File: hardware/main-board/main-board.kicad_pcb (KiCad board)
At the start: 4 copper layers, 105 x 38 mm, 99 parts, among them J1 USB_C_Receptacle_USB2.0, J2 DNI, J3 Display Connector, J4 Conn_01x04, SW1 SW_Push, SW2 SW_Push, SW3 SW_Push, SW4 SW_Push, SW5 SW_Detect, SW6 SW_Boot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

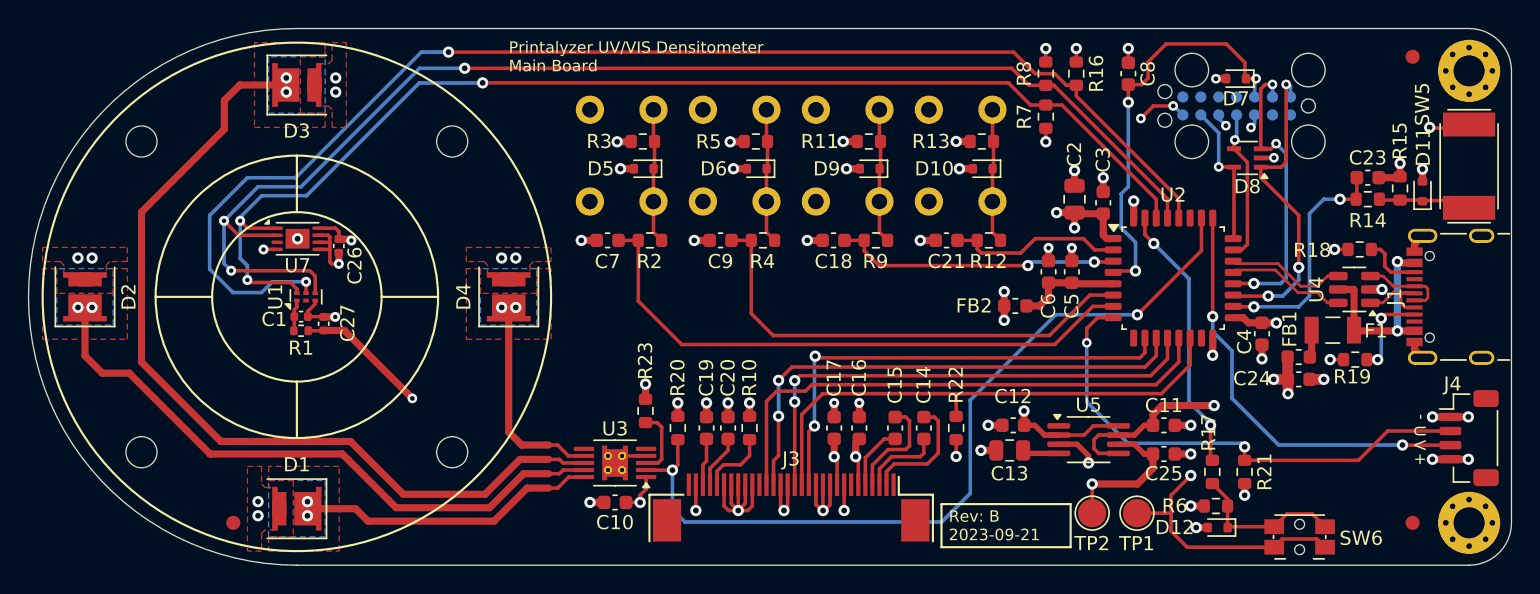
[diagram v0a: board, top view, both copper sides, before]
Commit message: Update main board to match common conventions from current projects
Changed all single-line TVS diodes to the ESD321
Changed ferrite beads to the new common part.
Added a 10nF filter capacitor to VBus.
Made all 10nF filter capacitors now 0603 sized.
Changed all vias to new common sizes.
Changed zone clearance settings to new common values.
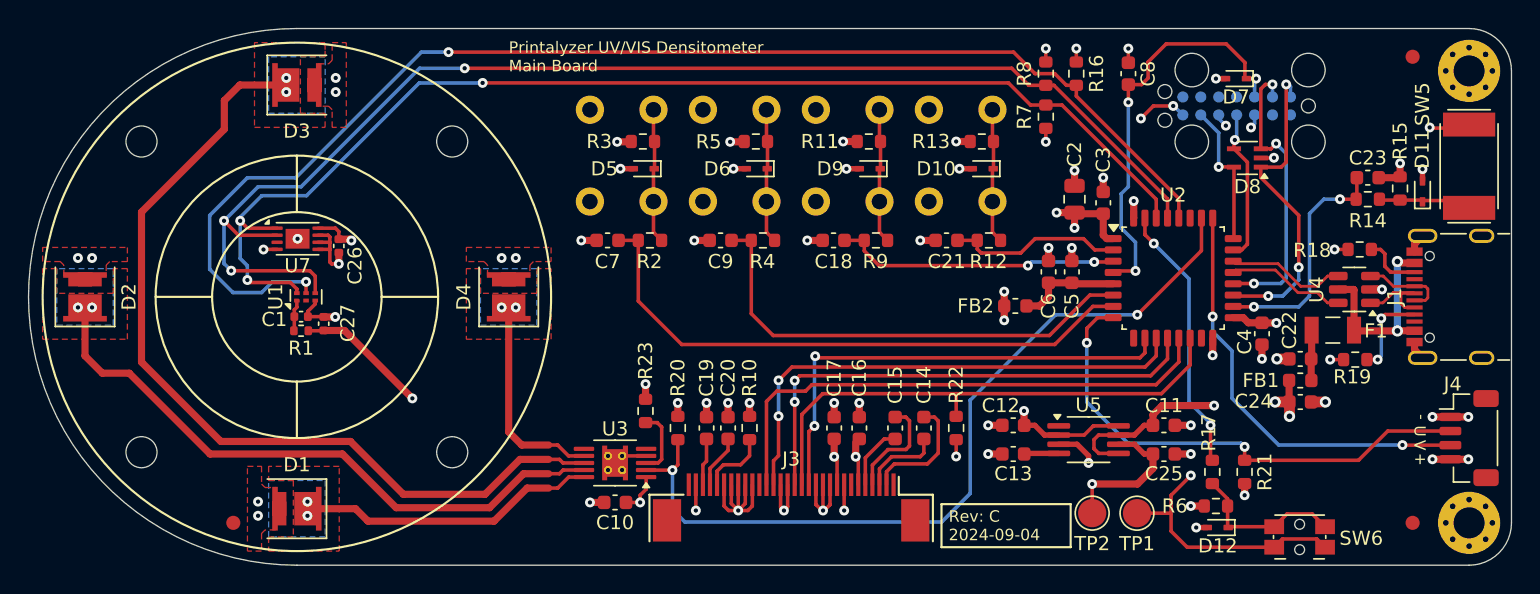
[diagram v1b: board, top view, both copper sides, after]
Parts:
- added C22: 10nF, Capacitor_SMD:C_0603_1608Metric, F.Cu at (131.0, 64.4)
- C13: footprint Capacitor_SMD:C_0805_2012Metric -> Capacitor_SMD:C_0603_1608Metric
- D10, D11, D12, D5, D6, D7, D9: value uClamp0501H -> ESD321; footprint Diode_SMD:D_SOD-523 -> lib_fp:D_TI_SOD-523_DYA0002A
- FB1, FB2: value 600R@100MHz -> 600R
- moved FB1 1.66 mm to (131.0, 65.9), turned to 180 degrees
- moved C24 1.61 mm to (131.0, 67.4)
- moved C13 0.36 mm to (110.7, 71.1)
- turned FB2 to 180 degrees
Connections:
- F1 pad 1: Net-(F1-Pad1) -> Net-(C22-Pad2)
- FB1 pad 1: +5V -> Net-(C22-Pad2)
- FB1 pad 2: Net-(F1-Pad1) -> +5V
- FB2 pad 1: +3.3V -> +3.3VA
- FB2 pad 2: +3.3VA -> +3.3V
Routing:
- net Net-(C22-Pad2): track 0.00 -> 3.29 mm
- net Net-(F1-Pad1): track 1.78 -> 0.00 mm
- net GND: track 94.0 -> 94.5 mm, vias 59 -> 60

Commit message: Split schematic into multiple files
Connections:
- net /RLED1 renamed /Sensor Head/RLED1
- net /RLED2 renamed /Sensor Head/RLED2
- net /RLED3 renamed /Sensor Head/RLED3
- net /RLED4 renamed /Sensor Head/RLED4

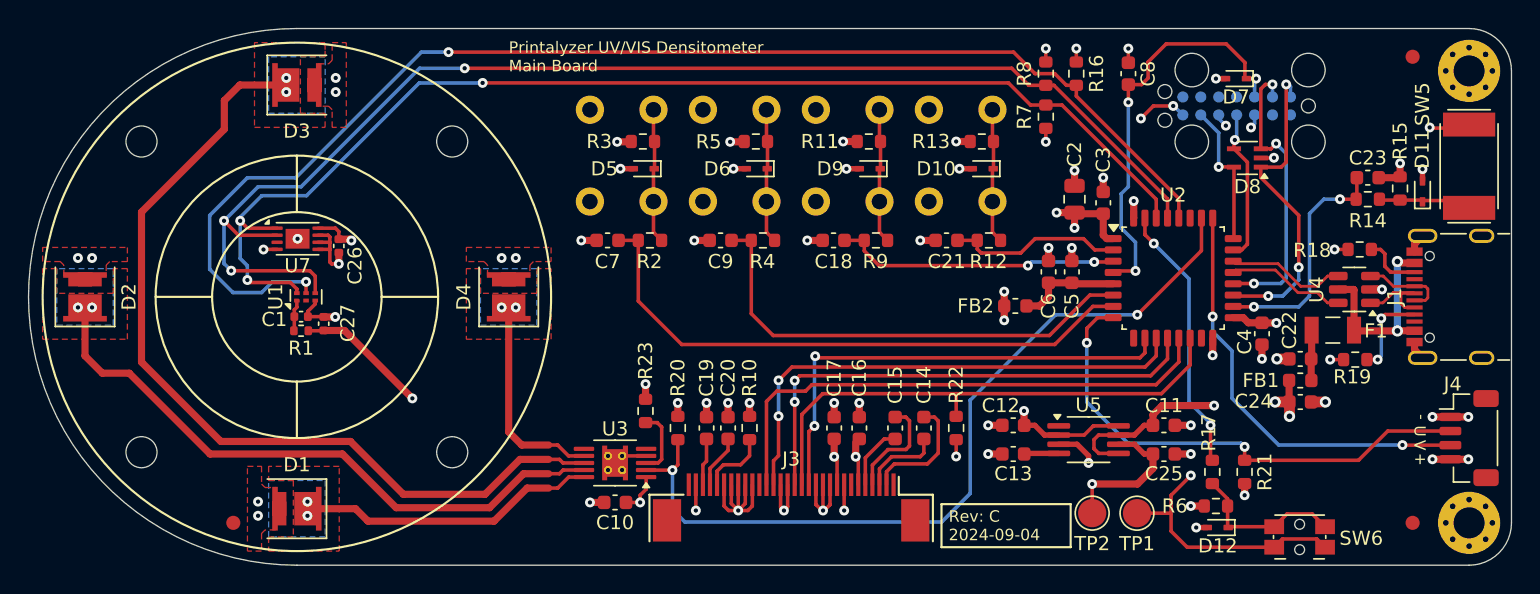
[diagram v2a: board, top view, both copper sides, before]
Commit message: Implement VSYNC reference signal
Adds a 32.768kHz oscillator and a binary counter to divide it, providing
a stable 128Hz signal routed to the sensor's VSYNC pin.
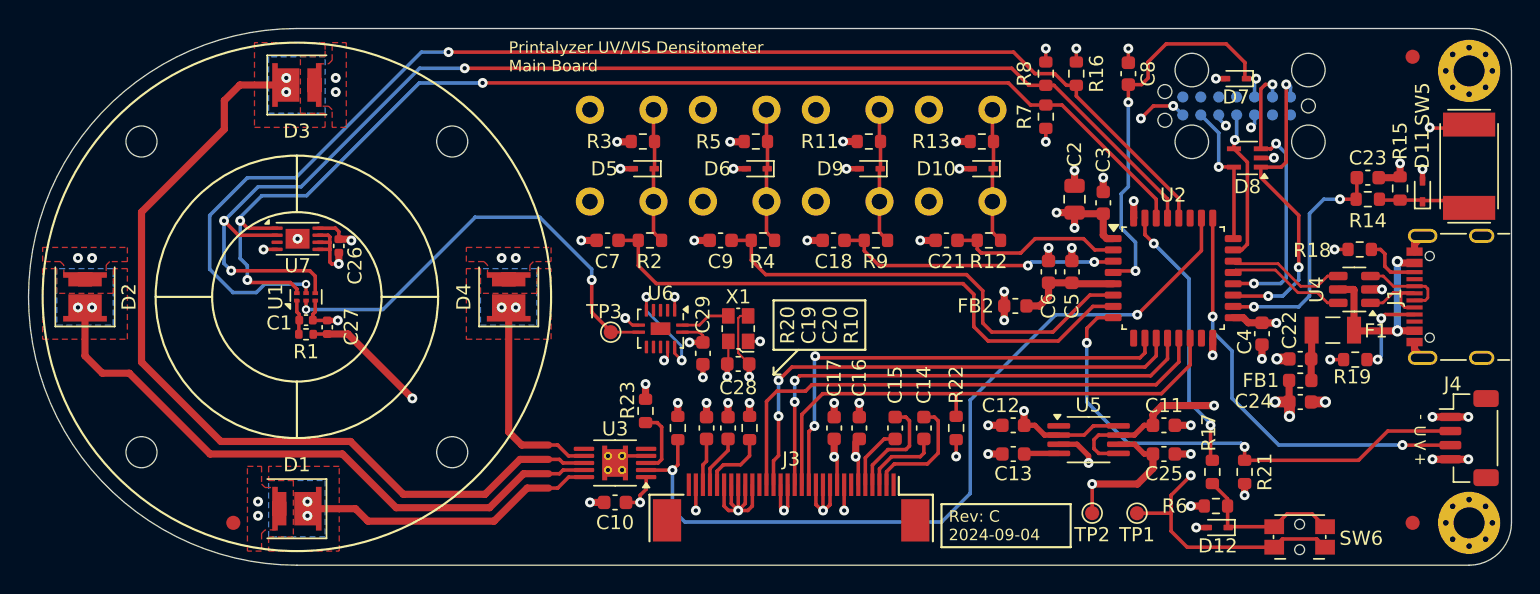
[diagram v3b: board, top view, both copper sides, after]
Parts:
- added C28: 0.1uF, Capacitor_SMD:C_0603_1608Metric, F.Cu at (91.2, 64.8)
- added C29: 0.1uF, Capacitor_SMD:C_0603_1608Metric, F.Cu at (88.8, 64.0)
- added TP3: 1.8V, TestPoint:TestPoint_Pad_D1.0mm, F.Cu at (82.2, 62.5)
- added U6: 74HC393, lib_fp:DHVQFN-14-1EP_2.5x3mm_P0.5mm_EP1x1.5mm, F.Cu at (85.8, 62.2)
- added X1: 327MVATX, lib_fp:Oscillator_SMD_ECS_327MVATX-2-4Pin_2.5x2.0mm, F.Cu at (91.2, 62.2)
- TP1, TP2: footprint TestPoint:TestPoint_Pad_D2.0mm -> TestPoint:TestPoint_Pad_D1.0mm
- moved C1 0.43 mm to (60.6, 61.6)
- moved R1 0.43 mm to (60.6, 62.6)
- moved C27 0.35 mm to (62.1, 62.1)
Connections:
- U1 pad 2: unconnected-(U1-VSYNC/GPIO-Pad2) -> /Sensor Head/TSL_VSYNC
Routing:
- net /Sensor Head/TSL_VSYNC: track 0.00 -> 32.1 mm, vias 0 -> 2
- net GND: track 94.5 -> 103.8 mm, vias 60 -> 65
- net Net-(U6A-Q3): track 0.00 -> 7.64 mm, vias 0 -> 2
- net +3.3V: track 54.9 -> 61.4 mm, vias 15 -> 18
- net Net-(U6A-CP): track 0.00 -> 3.52 mm
- net /BTN2: track 34.0 -> 33.0 mm

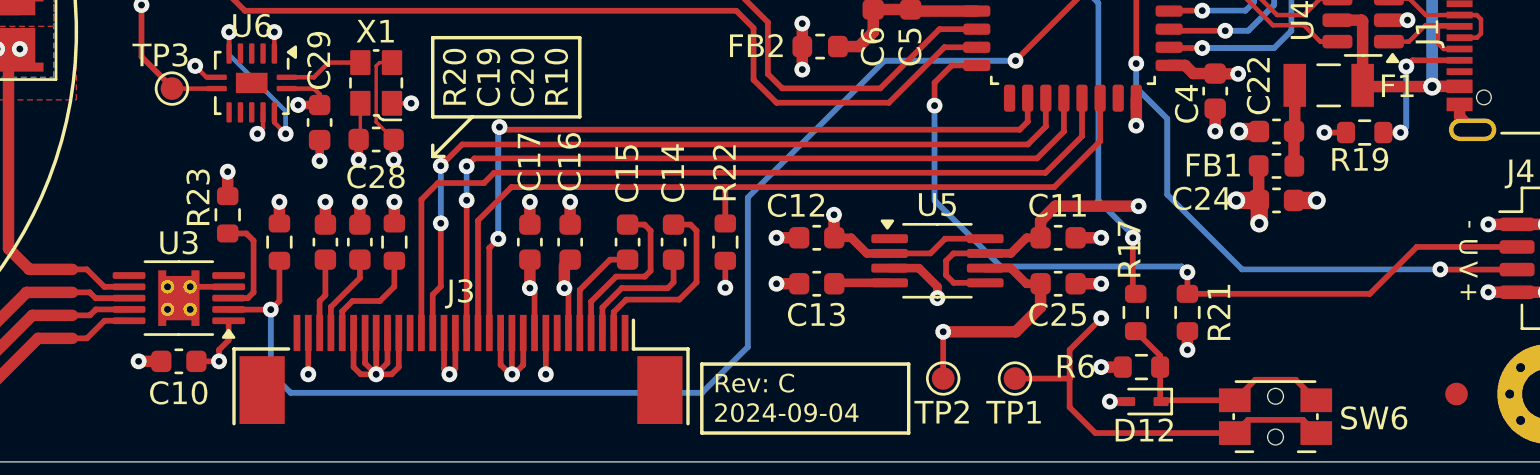
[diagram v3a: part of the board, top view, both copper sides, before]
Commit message: Fix various solder paste and silkscreen issues
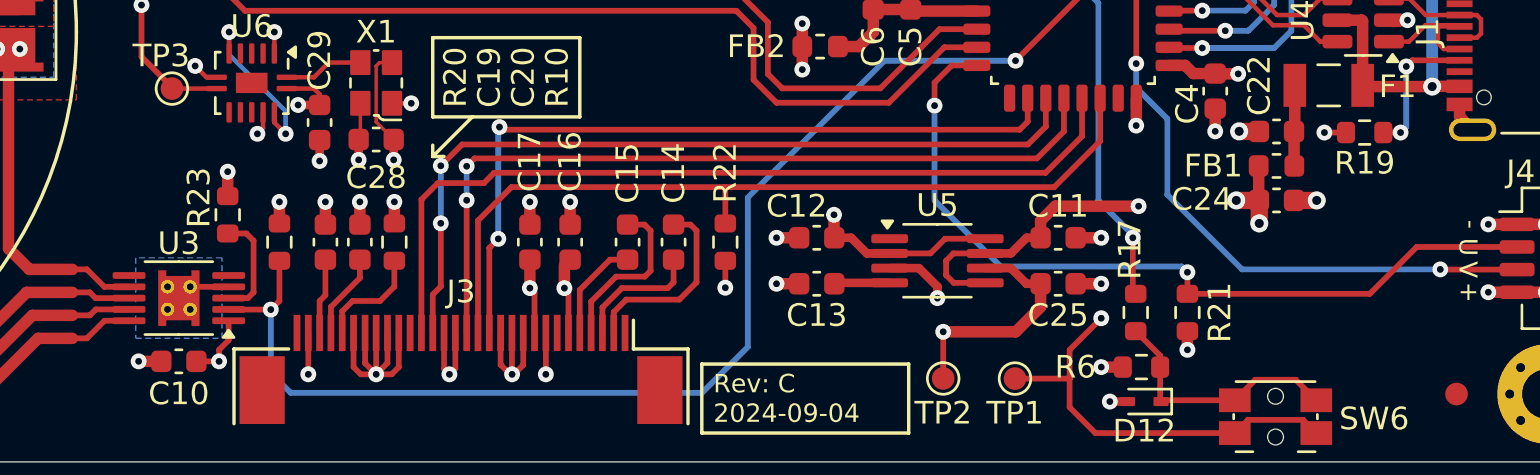
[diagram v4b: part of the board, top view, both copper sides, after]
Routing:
- added copper zone on B.Cu, net GND
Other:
- rule pad_to_mask_clearance: 0.05 -> 0
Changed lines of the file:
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@@
 			(dielectric_constraints yes)
 		)
-		(pad_to_mask_clearance 0.05)
+		(pad_to_mask_clearance 0)
+		(pad_to_paste_clearance -0.05)
 		(allow_soldermask_bridges_in_footprints no)
 		(aux_axis_origin 41 79)
@@
 		(sheetname "Root")
 		(sheetfile "main-board.kicad_sch")
-		(solder_paste_ratio -0.05)
+		(solder_paste_margin -0.025)
 		(attr smd)
 		(fp_line
@@
 		(sheetname "Input Buttons")
 		(sheetfile "main-board-buttons.kicad_sch")
+		(solder_paste_margin -0.025)
 		(attr smd)
 		(fp_line
@@
 		(sheetname "Input Buttons")
 		(sheetfile "main-board-buttons.kicad_sch")
+		(solder_paste_margin -0.025)
 		(attr smd)
 		(fp_line
@@
 		(sheetname "Input Buttons")
 		(sheetfile "main-board-buttons.kicad_sch")
+		(solder_paste_margin -0.025)
 		(attr smd)
 		(fp_line
@@
 		(sheetname "Input Buttons")
 		(sheetfile "main-board-buttons.kicad_sch")
+		(solder_paste_margin -0.025)
 		(attr smd)
 		(fp_line
@@
 		(sheetname "Input Buttons")
 		(sheetfile "main-board-buttons.kicad_sch")
+		(solder_paste_margin -0.025)
 		(attr smd)
 		(fp_line
@@
 		(sheetname "Root")
 		(sheetfile "main-board.kicad_sch")
+		(solder_paste_margin -0.025)
 		(attr smd)
 		(fp_line
@@
 		(tags "resistor")
 		(property "Reference" "R19"
-			(at 0.213 -1.222 0)
+			(at 0 -1.349 0)
 			(layer "F.SilkS")
 			(effects
@@
 		(sheetname "Root")
 		(sheetfile "main-board.kicad_sch")
-		(solder_paste_ratio -0.05)
+		(solder_paste_margin -0.025)
 		(attr smd)
 		(fp_line
@@
 		(sheetname "Root")
 		(sheetfile "main-board.kicad_sch")
-		(solder_paste_ratio -0.05)
 		(attr smd)
 		(fp_line
@@
 		(sheetname "Root")
 		(sheetfile "main-board.kicad_sch")
-		(solder_paste_ratio -0.05)
 		(attr smd)
 		(fp_line
@@
 		(sheetname "Input Buttons")
 		(sheetfile "main-board-buttons.kicad_sch")
+		(solder_paste_margin -0.025)
 		(attr smd)
 		(fp_line
@@
 		(sheetname "Sensor Head")
 		(sheetfile "main-board-sensor.kicad_sch")
+		(solder_paste_margin -0.025)
 		(zone_connect 2)
 		(attr smd)
@@
 		(sheetname "Root")
 		(sheetfile "main-board.kicad_sch")
-		(solder_paste_ratio -0.05)
 		(attr smd)
 		(fp_line
@@
 		(sheetname "Sensor Head")
 		(sheetfile "main-board-sensor.kicad_sch")
+		(solder_paste_margin -0.025)
 		(attr smd)
 		(fp_line
@@
 	(gr_line
 		(start 109.71 72.01)
-		(end 80.29 72.01)
+		(end 83.604 72.01)
 		(stroke
 			(width 0.1524)
@@
 		(layer "B.SilkS")
 	)
+	(gr_line
+		(start 80.29 72.01)
+		(end 81.454 72.015)
+		(stroke
+			(width 0.1524)
+			(type default)
+		)
+		(layer "B.SilkS")
+	)
 	(gr_circle
 		(center 60 60)
@@
 			)
 		)
+	)
+	(zone
+		(net 1)
+		(net_name "GND")
+		(layer "B.Cu")
+		(hatch edge 0.5)
+		(priority 8)
+		(connect_pads
+			(clearance 0.25)
+		)
+		(min_thickness 0.25)
+		(filled_areas_thickness no)
+		(fill yes
+			(thermal_gap 0.5)
+			(thermal_bridge_width 0.5)
+		)
+		(polygon
+			(pts
+				(xy 80.624 69.983) (xy 80.624 73.539) (xy 84.434 73.539) (xy 84.434 69.983)
+			)
+		)
